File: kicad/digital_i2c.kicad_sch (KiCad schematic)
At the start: 20 parts, among them J10 Qwiic EZO-pH, J11 Qwiic EZO-ORP, J12 Qwiic EZO-DO, J13 Qwiic EZO-RTD, J14 Load Cell, J7 Qwiic GPS SAM-M8Q, J8 Qwiic RTC DS3231, J9 Qwiic Cell Density, U13 MAX485ESA, U6 HX711

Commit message: fix: Embed lib_symbols, fix invalid lib_ids, bump to KiCad 9 format
- Embed complete (lib_symbols) definitions in all 5 sub-sheets so symbols
  render as real parts instead of '??' placeholders (files now self-contained)
- Substitute invalid lib_ids with valid library symbols:
  Device:CP -> Device:C_Polarized, Diode:PESD3V3S2USF -> Diode:PESD3V3S1UL,
  Diode:PESD5V0S1BSF -> Diode:PESD5V0S1UL, Isolator:PC817X2 -> Isolator:PC817
- Bump file format version 20231120 -> 20250114 (removes 'older version' warning)
- Left-justify header text blocks so long lines stay within the A3 frame

Validated: kicad-cli SVG render (all real symbols, within frame), clean-room
eeschema GUI render with broken library table (no '??'), and kicad-cli ERC
runs without crashing (425 violations are expected unconnected-pin/dangling-
label items, resolved during per-sheet wiring).

Co-Authored-By: Devin AI <158243242+devin-ai-integration[bot]@users.noreply.github.com>
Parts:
- C20: symbol Device:CP -> Device:C_Polarized
- D7_D8: symbol Diode:PESD3V3S2USF -> Diode:PESD3V3S1UL
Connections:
- net HX711_DOUT: now also U6.6 (INB-)
- net HX711_SCK: now also U6.10 (XI)
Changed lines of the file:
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@@
 (kicad_sch
-  (version 20231120)
+  (version 20250114)
   (generator "devin")
   (generator_version "1.0")
@@
   (text "I2C BUS — 400 kHz Fast Mode\nPull-ups 4.7k to 3.3V, ESD protection PESD3V3S2USF"
     (at 25.4 25.4 0)
-    (effects (font (size 2.54 2.54)))
+    (effects (font (size 2.54 2.54)) (justify left))
   )
   (symbol
@@
   )
   (symbol
-    (lib_id "Diode:PESD3V3S2USF")
+    (lib_id "Diode:PESD3V3S1UL")
     (at 50.8 58.42 0) (unit 1)
     (exclude_from_sim no) (in_bom yes) (on_board yes)
@@
   (text "HX711 LOAD CELL ADC\n24-bit, Gain 128, 80 SPS\nD2=DOUT, D3=SCK"
     (at 170.18 25.4 0)
-    (effects (font (size 2.54 2.54)))
+    (effects (font (size 2.54 2.54)) (justify left))
   )
   (symbol
@@
   )
   (symbol
-    (lib_id "Device:CP")
+    (lib_id "Device:C_Polarized")
     (at 177.8 68.58 0) (unit 1)
     (exclude_from_sim no) (in_bom yes) (on_board yes)

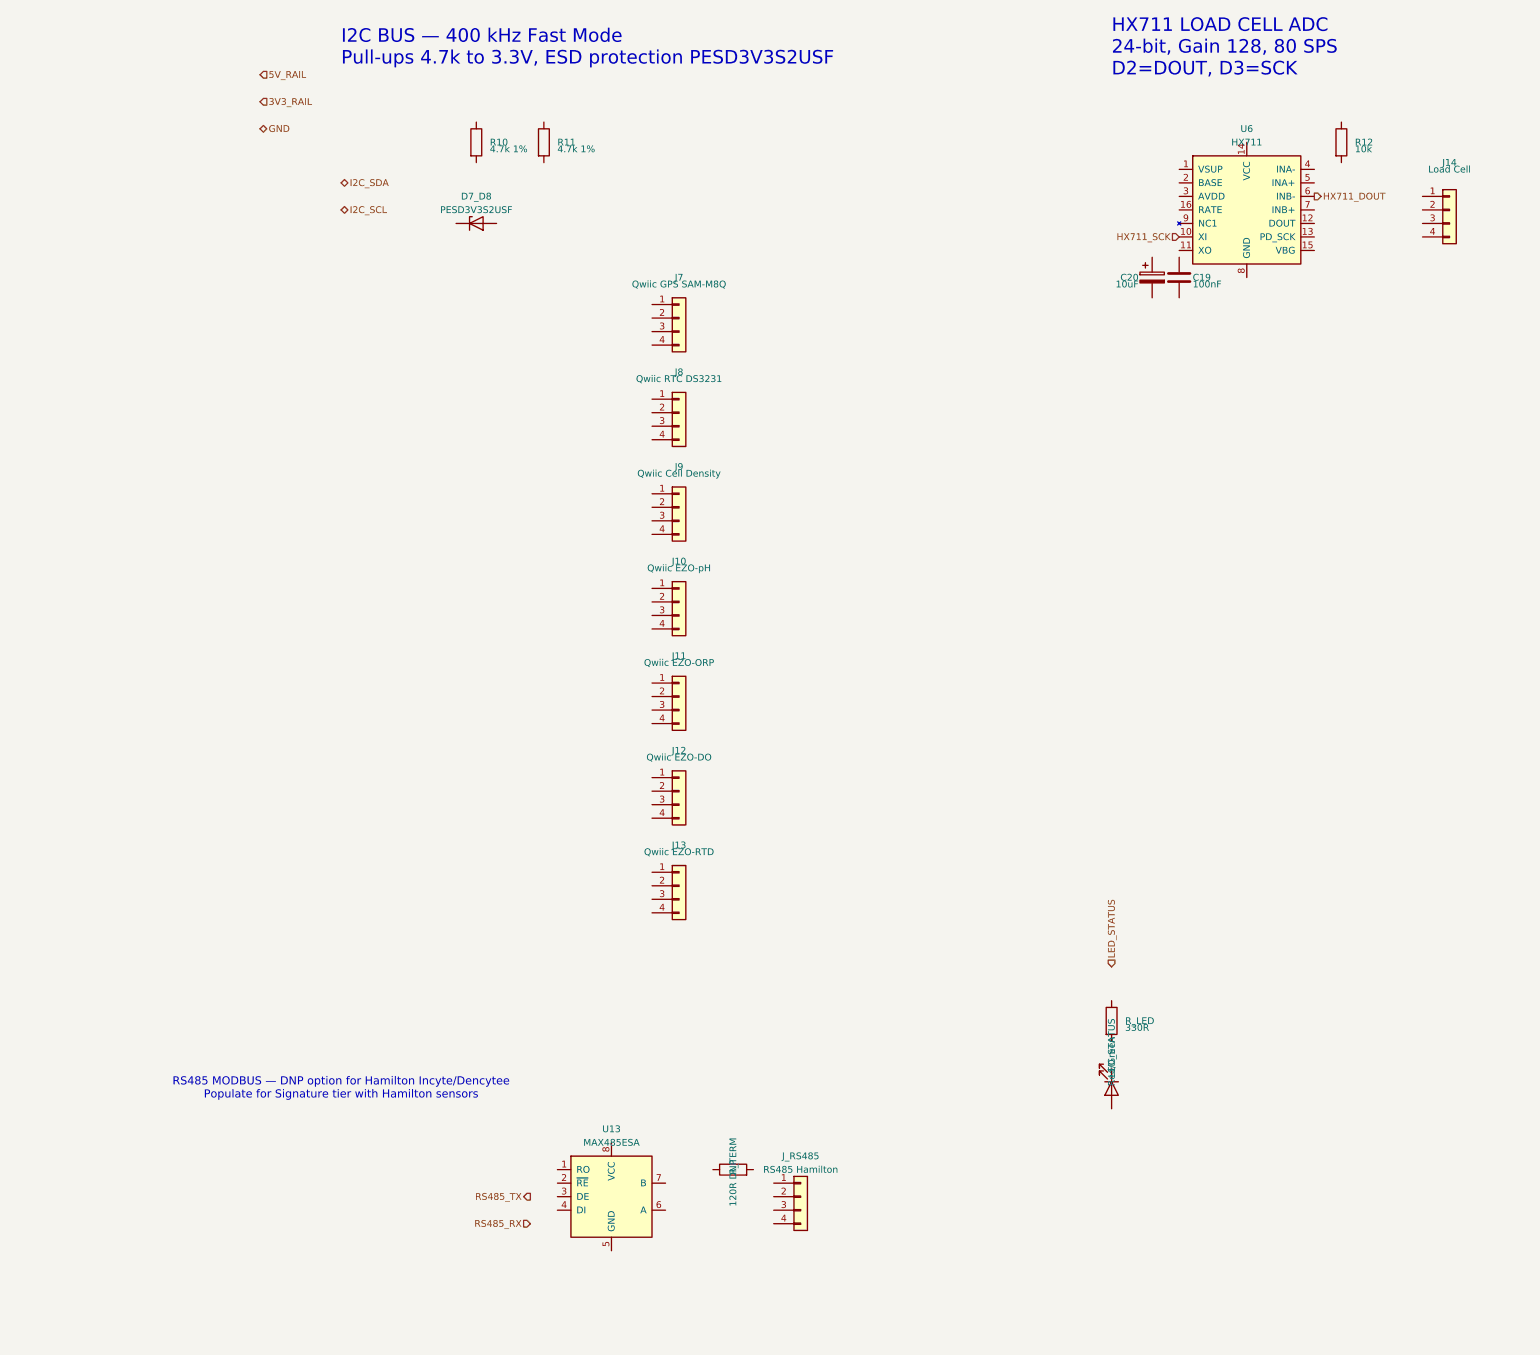
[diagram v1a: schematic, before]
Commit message: fix: Re-annotate components with unique global references + add instances blocks
Root cause: symbol instances lacked (instances ...) blocks, so KiCad treated
all references as unannotated/duplicated (108 duplicate_reference ERC errors)
and produced auto-renamed names (C_DO2, U3_2A, ...) on annotation.

Fix: assign globally-unique sequential standard references (R1..R28, C1..C27,
U1..U20, D1..D18, J1..J21, etc.) and embed a proper (instances) block per
symbol with the correct hierarchical path. Each MCP6002 kept as its own IC
(unit A) to preserve per-channel galvanic isolation (pH/ORP/DO).

ERC: duplicate_reference 108 -> 0, unannotated 1 -> 0.
Co-Authored-By: Devin AI <158243242+devin-ai-integration[bot]@users.noreply.github.com>
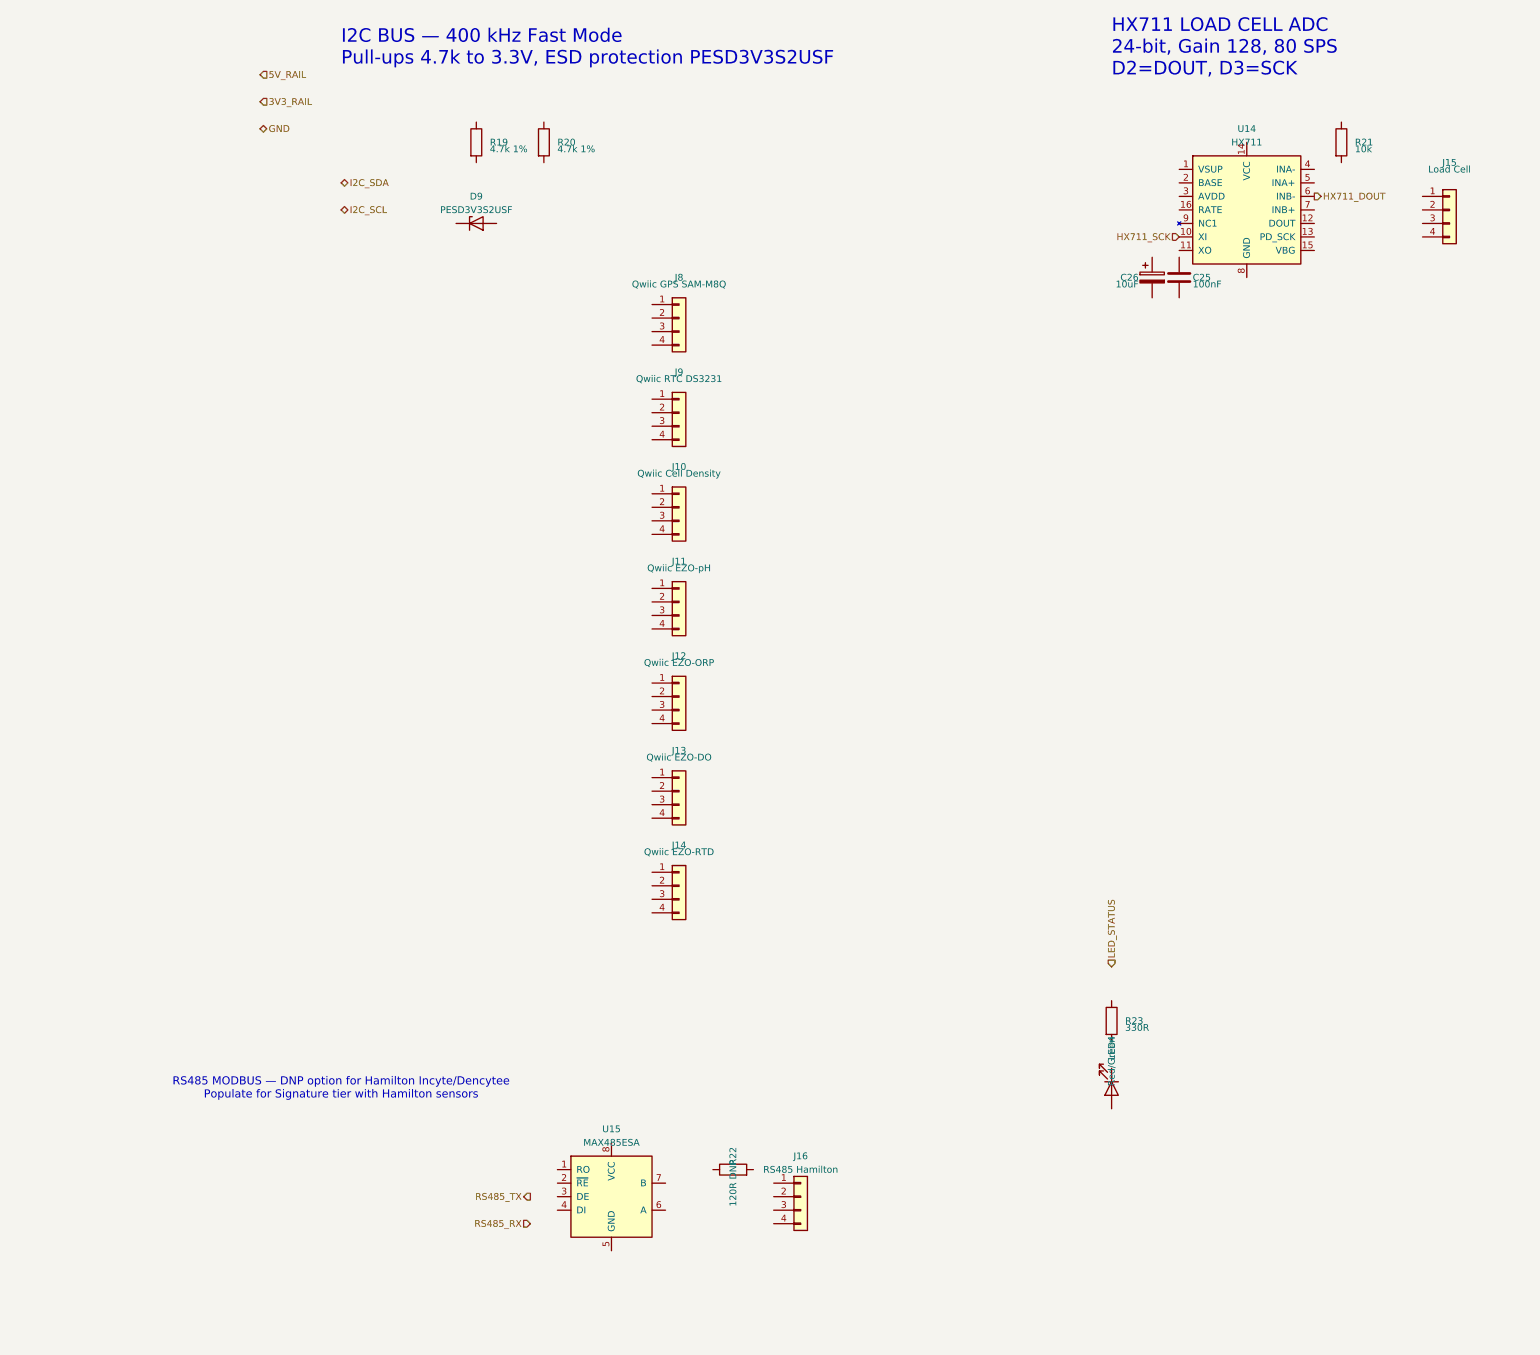
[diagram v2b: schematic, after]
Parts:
- renumbered C19 to C25, C20 to C26, D7_D8 to D9, J9 to J10, J10 to J11, J11 to J12, J12 to J13, J13 to J14, J14 to J15, J_RS485 to J16, J7 to J8, J8 to J9, LED_STATUS to LED4, R10 to R19, R11 to R20, R12 to R21, R_TERM to R22, R_LED to R23, U6 to U14, U13 to U15

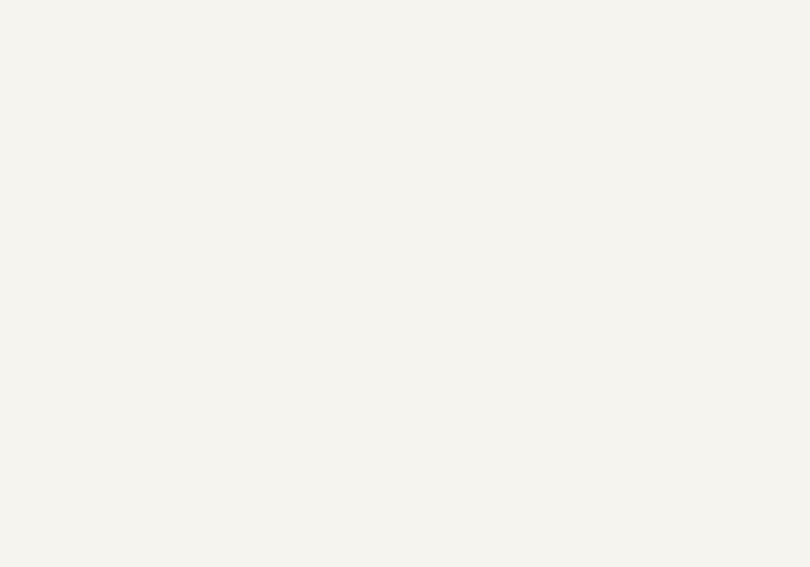
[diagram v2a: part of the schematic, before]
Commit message: fix: reconcile refdes across schematic, BOM, and netlist doc
BOM completely rewritten to match schematic refdes (source of truth):
- U3=TPS3823 (was U12), U4/U7/U10/U11=MCP6002 (was U3 qty2)
- U5/U8/U12=SN6501, U6/U9/U13=AMC1301 (replaces ADuM1250)
- U14=HX711 (was U6), U15=MAX485 (was U13)
- U16=PC817X2, U17=IR2104 (was U7), U18/U19=PC817X1
- R3=WDI pull-up (was R_WDI), R4-R6=LED limits (was R_LED1-3)
- R19/R20=I2C pull-ups (was R10/R11), R21=HX711 pull-up (was R12)
- R24-R27=opto limits (was R13-R20), R28/C27/U20=CO2 PWM (was R21/C22/U3C)
- All connectors shifted: J1=barrel jack, J2-J7=analog, J8-J16=digital
- Added T1-T3, D19-D24, C28-C30 (isolated supply components)

Netlist doc (07_KICAD_NETLIST.md) Rev 2.0:
- All refdes updated to match schematic
- ADC mapping follows firmware: A2=Temp, A3=Hum, A4=CO2, A5=DO
- HX711 on 3V3_RAIL (no level-shift)
- Architecture B2 (AMC1301) documented with isolated supply topology

Schematic additions:
- U21 (ISO1541DR) added to digital_i2c for Atlas EZO I2C isolation
- J22 (Terminal 2P) added to actuator_drivers for CO2 valve output

Co-Authored-By: Devin AI <158243242+devin-ai-integration[bot]@users.noreply.github.com>
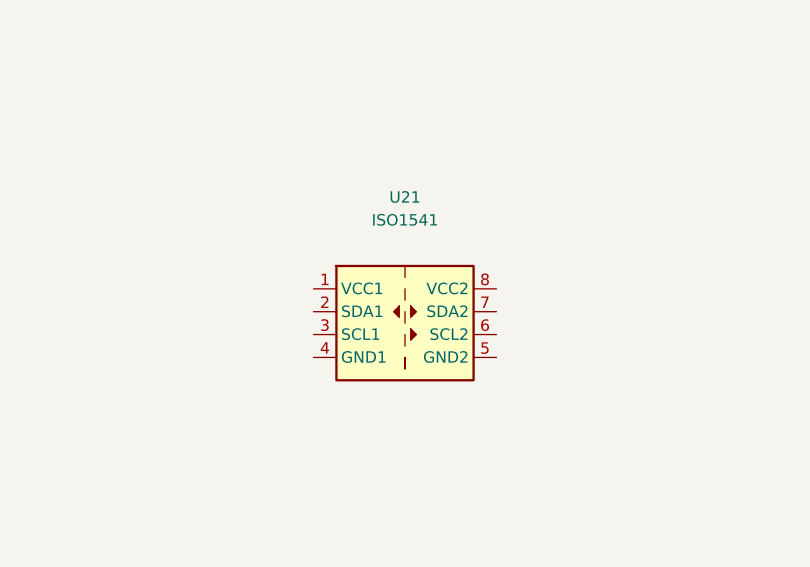
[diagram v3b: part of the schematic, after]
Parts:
- added U21: ISO1541, Package_SO:SOIC-8_3.9x4.9mm_P1.27mm, symbol Isolator:ISO1541
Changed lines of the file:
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@@
   (hierarchical_label "5V_RAIL"     (shape input)  (at 10.16 30.48 0)        (effects (font (size 1.27 1.27))))
   (hierarchical_label "GND"         (shape bidirectional) (at 10.16 40.64 0) (effects (font (size 1.27 1.27))))
+  (symbol (lib_id "Isolator:ISO1541") (at 149.86 121.92 0) (unit 1) (exclude_from_sim no) (in_bom yes) (on_board yes)
+    (property "Reference" "U21" (at 149.86 109.22 0) (effects (font (size 1.27 1.27))))
+    (property "Value" "ISO1541" (at 149.86 111.76 0) (effects (font (size 1.27 1.27))))
+    (property "Footprint" "Package_SO:SOIC-8_3.9x4.9mm_P1.27mm" (at 149.86 121.92 0) (effects (font (size 1.27 1.27)) hide))
+    (property "Datasheet" "https://www.ti.com/lit/ds/symlink/iso1541.pdf" (at 149.86 121.92 0) (effects (font (size 1.27 1.27)) hide))
+    (property "MPN" "ISO1541DR" (at 149.86 121.92 0) (effects (font (size 1.27 1.27)) hide))
+    (property "Distributor_PN" "296-ISO1541DRCT-ND" (at 149.86 121.92 0) (effects (font (size 1.27 1.27)) hide))
+    (instances
+      (project "nebula_qshield"
+        (path "/c6da75fc-541f-4933-b134-f5eb8982a11b/43ec48b6-2639-4f87-888d-e2ac5bc6a498"
+          (reference "U21") (unit 1)
+        )
+      )
+    )
+  )
 )
